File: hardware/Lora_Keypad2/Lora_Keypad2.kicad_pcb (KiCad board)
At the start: 2 copper layers, 54 x 76.2 mm, 9 parts, among them J1 OLED Conn

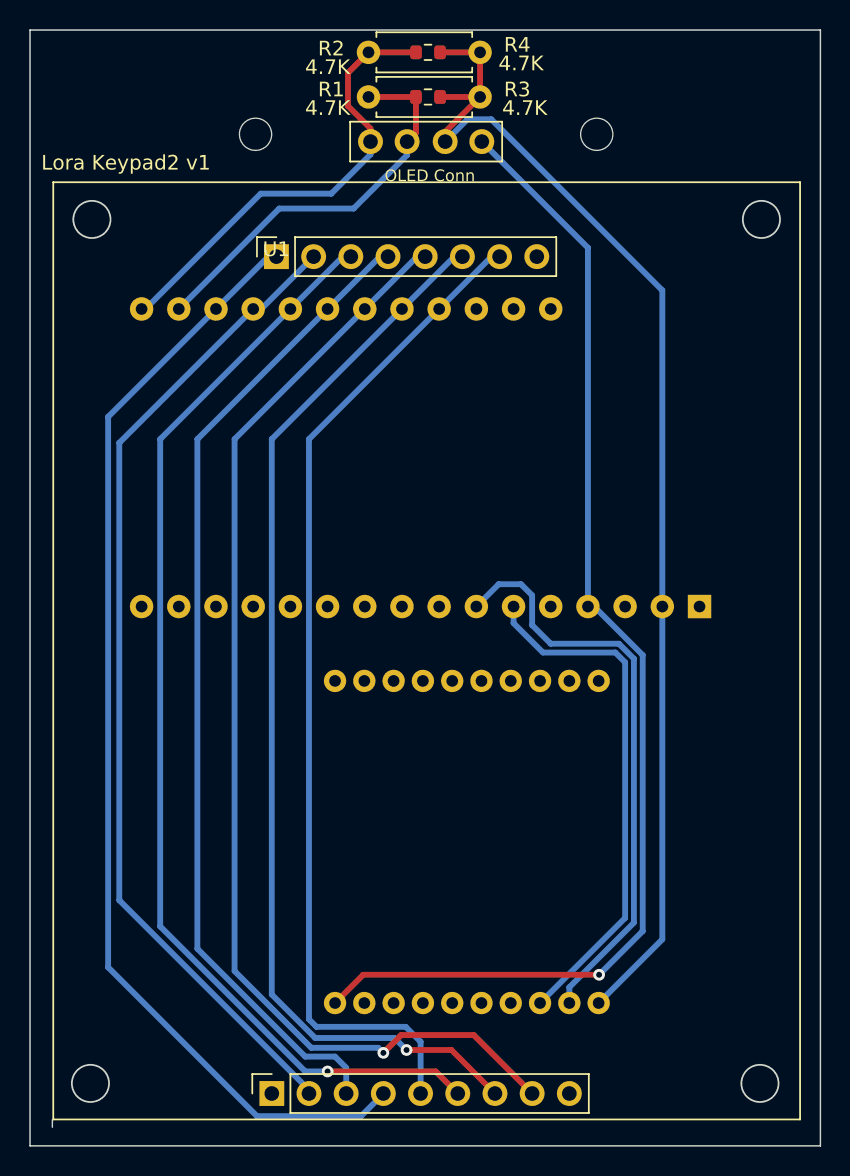
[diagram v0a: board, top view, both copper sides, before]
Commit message: working on case for hw2
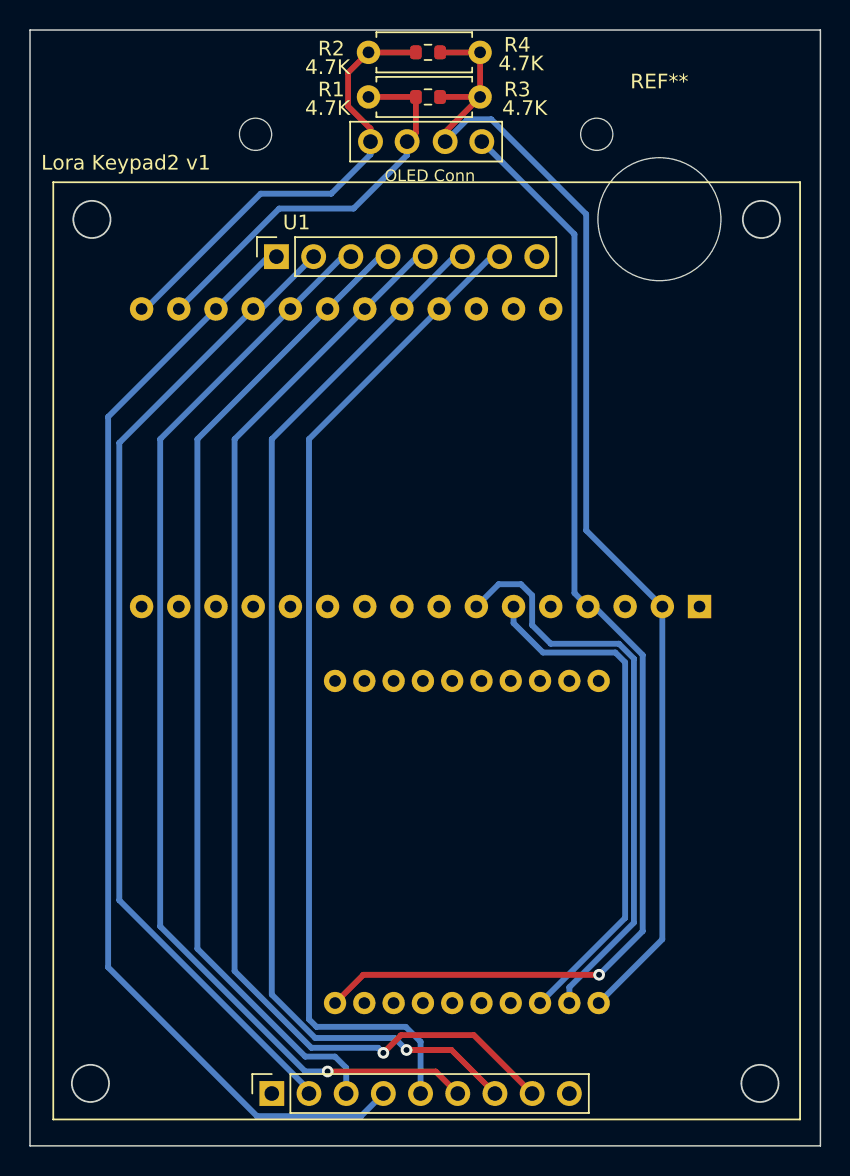
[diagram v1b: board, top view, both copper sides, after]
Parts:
- added REF**: MountingHole_8.4mm_M8, MountingHole:MountingHole_8.4mm_M8, F.Cu at (215.7, 68.8)
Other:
- outline, holes or cut-outs redrawn
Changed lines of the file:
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@@
     )
+  )
+  (footprint "MountingHole:MountingHole_8.4mm_M8" (layer "F.Cu")
+    (at 215.7 68.8)
+    (descr "Mounting Hole 8.4mm, no annular, M8")
+    (tags "mounting hole 8.4mm no annular m8")
+    (attr exclude_from_pos_files exclude_from_bom)
+    (fp_text reference "REF**" (at 0 -9.4) (layer "F.SilkS")
+        (effects (font (size 1 1) (thickness 0.15)))
+    )
+    (fp_text value "MountingHole_8.4mm_M8" (at 0 9.4) (layer "F.Fab")
+        (effects (font (size 1 1) (thickness 0.15)))
+    )
+    (fp_text user "${REFERENCE}" (at 0 0) (layer "F.Fab")
+        (effects (font (size 1 1) (thickness 0.15)))
+    )
+    (fp_circle (center 0 0) (end 8.4 0)
+      (stroke (width 0.15) (type solid)) (fill none) (layer "Cmts.User"))
+    (fp_circle (center 0 0) (end 8.65 0)
+      (stroke (width 0.05) (type solid)) (fill none) (layer "F.CrtYd"))
+    (pad "" np_thru_hole circle (at 0 0) (size 8.4 8.4) (drill 8.4) (layers "*.Cu" "*.Mask"))
   )
   (footprint "keypad:3x4_keypad" (layer "F.Cu")
@@
     (property "Sheetname" "")
     (attr through_hole exclude_from_pos_files exclude_from_bom)
-    (fp_text reference "U1" (at 0 -0.5 unlocked) (layer "F.SilkS")
+    (fp_text reference "U1" (at 1.3775 -2.33 unlocked) (layer "F.SilkS")
         (effects (font (size 1 1) (thickness 0.15)))
     )
@@
     )
   )
+  (gr_line (start 174.244 130.302) (end 174.244 130.81)
+    (stroke (width 0.1) (type default)) (layer "Dwgs.User"))
   (gr_line (start 172.72 132.08) (end 172.72 55.88)
     (stroke (width 0.1) (type default)) (layer "Edge.Cuts"))
@@
     (stroke (width 0.1) (type default)) (layer "Edge.Cuts"))
   (gr_line (start 226.695 55.88) (end 226.695 132.08)
-    (stroke (width 0.1) (type default)) (layer "Edge.Cuts"))
-  (gr_line (start 174.244 130.302) (end 174.244 130.81)
     (stroke (width 0.1) (type default)) (layer "Edge.Cuts"))
   (gr_text "${TITLE} ${REVISION}" (at 173.482 65.532) (layer "F.SilkS")
@@
   (segment (start 200.723 60.452) (end 203.454 60.452) (width 0.4) (layer "F.Cu") (net 2))
   (segment (start 204.216 61.976) (end 202.595 61.976) (width 0.4) (layer "B.Cu") (net 2))
+  (segment (start 215.9 95.25) (end 210.7 90.05) (width 0.4) (layer "B.Cu") (net 2))
   (segment (start 215.9 117.97792) (end 211.55152 122.3264) (width 0.4) (layer "B.Cu") (net 2))
-  (segment (start 215.9 95.25) (end 215.9 73.66) (width 0.4) (layer "B.Cu") (net 2))
+  (segment (start 210.7 90.05) (end 210.7 68.46) (width 0.4) (layer "B.Cu") (net 2))
+  (segment (start 210.7 68.46) (end 204.216 61.976) (width 0.4) (layer "B.Cu") (net 2))
   (segment (start 202.595 61.976) (end 201.071 63.5) (width 0.4) (layer "B.Cu") (net 2))
-  (segment (start 215.9 73.66) (end 204.216 61.976) (width 0.4) (layer "B.Cu") (net 2))
   (segment (start 215.9 95.25) (end 215.9 117.97792) (width 0.4) (layer "B.Cu") (net 2))
   (segment (start 195.48094 120.396) (end 193.55054 122.3264) (width 0.4) (layer "F.Cu") (net 4))
@@
   (via (at 211.582 120.396) (size 0.8) (drill 0.4) (layers "F.Cu" "B.Cu") (net 4))
   (segment (start 214.56 98.562944) (end 214.56 117.418) (width 0.4) (layer "B.Cu") (net 4))
+  (segment (start 203.571 63.5) (end 209.9 69.829) (width 0.4) (layer "B.Cu") (net 4))
+  (segment (start 209.9 69.829) (end 209.9 94.33) (width 0.4) (layer "B.Cu") (net 4))
   (segment (start 210.82 95.25) (end 211.247056 95.25) (width 0.4) (layer "B.Cu") (net 4))
   (segment (start 214.56 117.418) (end 211.582 120.396) (width 0.4) (layer "B.Cu") (net 4))
   (segment (start 211.247056 95.25) (end 214.56 98.562944) (width 0.4) (layer "B.Cu") (net 4))
-  (segment (start 210.82 70.749) (end 210.82 95.25) (width 0.4) (layer "B.Cu") (net 4))
-  (segment (start 203.571 63.5) (end 210.82 70.749) (width 0.4) (layer "B.Cu") (net 4))
+  (segment (start 209.9 94.33) (end 210.82 95.25) (width 0.4) (layer "B.Cu") (net 4))
   (segment (start 194.437 58.801) (end 194.437 61.077) (width 0.4) (layer "F.Cu") (net 15))
   (segment (start 195.971 62.611) (end 195.971 63.5) (width 0.4) (layer "F.Cu") (net 15))
